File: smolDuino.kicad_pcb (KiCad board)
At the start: 2 copper layers, 68.6 x 53.3 mm, 63 parts, among them J1 Barrel_Jack_Switch, J2 USB_C_Receptacle_USB2.0, J3 2x3 SPI Header, J4 2x5 HV Outputs, J5 I^{2}C Connector, P1 CONN_01X01, P2 CONN_01X01, P3 CONN_01X01, P4 CONN_01X01, P5 Digital, P6 Power, P7 Digital, P8 Analog, Q1 AO3401A, SW1 Enable, SW2 Reset, U1 AP62250smol_A, U2 rp2040smol-c-unit, U3 74AHCT1G04, U4 Charj_smol, U5 AT24CS02-STUM, U6 SN74AHCT125N

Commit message: commit before I ruin too much
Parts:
- JP1: value 0 -> 0 DNP
- U6: footprint Package_DFN_QFN:Texas_S-PVQFN-N14 -> MikeFootprintLib:74x125_Texas_S-PVQFN-N14
- moved C4 0.29 mm to (141.9, 88.1)
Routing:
- net GND: track 89.1 -> 82.9 mm
- net /5V_IO15: track 6.67 -> 7.82 mm
- net /IO14: track 23.3 -> 24.3 mm
- net /EN: track 62.6 -> 62.1 mm
- net Net-(D3-Pad1): track 4.37 -> 4.90 mm

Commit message: Progress
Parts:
- removed the G*** at (174.0, 80.2)
- added C1: 47u, Capacitor_SMD:CP_Elec_6.3x5.4, F.Cu at (132.0, 121.9)
- added D4: Charge, LED_SMD:LED_0603_1608Metric, F.Cu at (127.9, 112.6)
- added R8: 2k, Resistor_SMD:R_0603_1608Metric, F.Cu at (142.7, 101.5)
- C2: renamed from C1; value 10uF -> 4u7
- C3: renamed from C2; value 100nF -> 100n
- C4, C5: value 100nF -> 100n
- D3: value Charge -> ChargeEn
- J1: value Barrel_Jack_Switch -> DC Barrel Jack
- U1: value AP62250smol_A -> AP62250smol; footprint MikePCBAs:AP62250smol_A -> MikePCBAs:AP62250smol_C
- moved SW1 46.5 mm to (176.5, 111.3), turned to 90 degrees
- moved MISC2 27.7 mm to (171.9, 111.2)
- moved ART1 23.6 mm to (174.0, 83.6)
- moved G*** 19.4 mm to (141.1, 118.9)
- moved D3 15.3 mm to (141.2, 101.5)
- moved G*** 8.49 mm to (125.0, 114.6)
- moved G*** 8.42 mm to (175.8, 103.9)
- moved R1 4.87 mm to (131.7, 108.3), turned to 180 degrees
- moved R3 4.38 mm to (128.7, 108.3), turned to 180 degrees
- moved F1 3.89 mm to (131.7, 113.6)
- moved R7 2.48 mm to (143.0, 107.3), turned to 90 degrees
- moved C6 2.30 mm to (140.4, 106.6), turned to 180 degrees
- moved U5 1.82 mm to (142.2, 104.4)
- moved JP1 1.18 mm to (129.4, 104.2)
- moved ART2 1.14 mm to (167.9, 106.2)
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- renumbered ART3 to ART2, ART4 to ART3, ART2 to ART4, C3 to C6, JP2 to JP1, JP3 to JP2, JP1 to JP3, R6 to R5, R7 to R6, R5 to R7, U6 to U3, U5 to U4, U3 to U5, U4 to U6
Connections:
- net Net-(C1-Pad2) renamed /V_{Bus}_{Fused}
- net Net-(F2-Pad1) renamed /V_{Bus}
- net Net-(J2-PadA5) renamed /CC1
- net Net-(J2-PadB5) renamed /CC2
- D3 pad 1: Net-(D3-Pad1) -> /~{ChargeEn}
- D3 pad 2: +5V -> Net-(D3-Pad2)
- U5 pad 4: Net-(U3-Pad4) -> /~{ChargeEn}
- U6 pad 5: Net-(U3-Pad4) -> /~{ChargeEn}
- U6 pad 6: Net-(D3-Pad1) -> /STAT
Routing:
- net /EN: track 62.1 -> 13.5 mm, vias 2 -> 0
- net /~{ChargeEn}: track 0.00 -> 28.9 mm, vias 0 -> 2
- net V_{High}: track 122.3 -> 145.2 mm
- net Net-(U3-Pad4): track 21.1 -> 0.00 mm
- net /VIN: track 35.0 -> 50.5 mm
- net /VIN_{Fused}: track 0.00 -> 12.9 mm
- net +5V: track 82.1 -> 91.8 mm
- net Net-(Q1-Pad1): track 51.7 -> 42.6 mm
- net /DC_{In}: track 12.3 -> 5.60 mm
- net V_{high_out}: track 18.2 -> 12.4 mm
- net Net-(D3-Pad1): track 4.90 -> 0.00 mm
- net /STAT: track 0.00 -> 3.80 mm
- net GND: track 82.9 -> 80.4 mm, vias 193 -> 201
- net /5V_MOSI1: track 23.4 -> 21.2 mm, vias 0 -> 1
- net /Reset: track 170.6 -> 172.6 mm
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- removed copper zone on F.Cu, net /VIN_{Fused}
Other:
- outline, holes or cut-outs redrawn

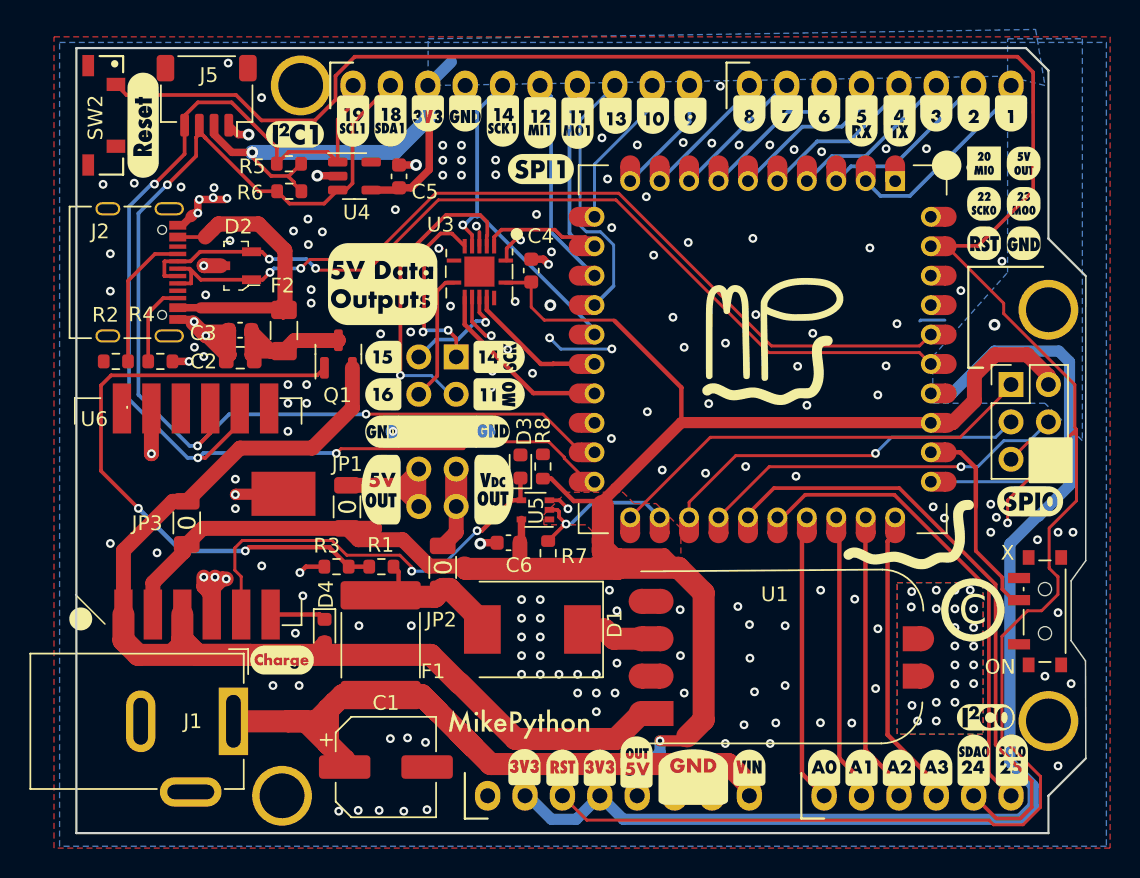
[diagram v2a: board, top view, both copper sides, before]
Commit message: More progress. Charjsmol is removed and integrated directly onto the board.
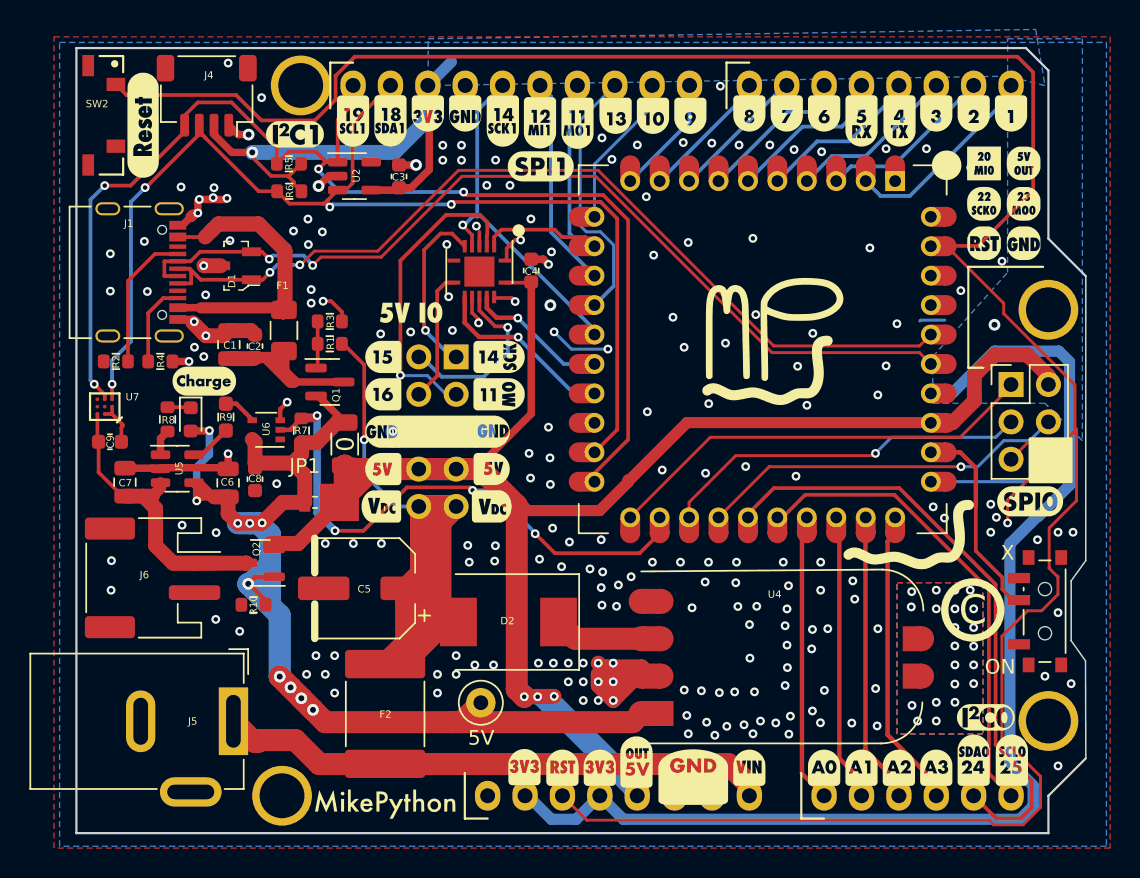
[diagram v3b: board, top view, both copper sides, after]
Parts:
- removed ART3, ART4: MPAnyArt, MikeArtworkLib:5vDataOutputsLabel
- removed the D3 at (141.2, 101.5)
- removed the JP1 at (129.4, 104.2)
- removed JP2: 0, MikeFootprintLib:R_0OHM_1206_3216Metric
- removed the U6 at (114.2, 111.5)
- added 5V: TestPoint, TestPoint:TestPoint_Loop_D2.50mm_Drill1.0mm_LowProfile, F.Cu at (138.5, 117.5)
- added C6: 10uF, Capacitor_SMD:C_0805_2012Metric, F.Cu at (121.3, 102.6)
- added C7: 10uF, Capacitor_SMD:C_0805_2012Metric, F.Cu at (114.3, 102.5)
- added C9: 1uF, Capacitor_SMD:C_0603_1608Metric, F.Cu at (113.3, 99.8)
- added D4: UPS120, MikeFootprintLib:UPS120_D_Powermite_AK, F.Cu at (128.2, 103.9)
- added G***: LOGO, LOGO, B.Cu at (135.5, 91.2)
- added G***: LOGO, LOGO, F.Cu at (134.0, 91.2)
- added J6: Battery Connector, Connector_JST:JST_PH_S2B-PH-SM4-TB_1x02-1MP_P2.00mm_Horizontal, F.Cu at (116.2, 109.0)
- added Q2: AO3401A, Package_TO_SOT_SMD:SOT-23, F.Cu at (123.5, 108.0)
- added R10: 100K, Resistor_SMD:R_0603_1608Metric, F.Cu at (123.0, 110.9)
- added R9: 4.7k, Resistor_SMD:R_0603_1608Metric_Pad0.98x0.95mm_HandSolder, F.Cu at (121.2, 98.1)
- added U5: MCP73831-2-OT, Package_TO_SOT_SMD:SOT-23-5, F.Cu at (117.8, 101.6)
- added U7: LC709203FXE-05MH, MikeFootprintLib:WLCSP9-1.60x1.76mm, F.Cu at (112.9, 97.4)
- R8: value 2k -> 1k
- U3: footprint MikeFootprintLib:74x125_Texas_S-PVQFN-N14 -> Package_DFN_QFN:Texas_S-PVQFN-N14
- moved R8 25.7 mm to (117.2, 98.3)
- moved G*** 19.7 mm to (119.7, 95.7)
- moved U6 19.1 mm to (123.9, 99.0)
- moved R7 18.7 mm to (126.3, 99.0)
- moved C8 17.8 mm to (123.1, 102.3), turned to -90 degrees
- moved D3 17.0 mm to (118.8, 98.3)
- moved R3 16.7 mm to (128.2, 91.6), turned to 0 degrees
- moved R1 15.5 mm to (128.2, 93.1)
- moved C5 12.2 mm to (130.6, 109.7), turned to 180 degrees
- moved JP1 12.0 mm to (129.2, 99.9), turned to 90 degrees
- moved G*** 10.6 mm to (132.0, 124.4)
- moved F2 4.68 mm to (132.0, 118.3)
- moved Q1 1.99 mm to (128.2, 95.7), turned to 0 degrees
- moved D2 1.70 mm to (140.4, 112.0)
- moved C2 1.48 mm to (123.1, 93.3), turned to 90 degrees
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- renumbered C2 to C1, C3 to C2, C5 to C3, C1 to C5, C6 to C8, D2 to D1, D1 to D2, D4 to D3, F2 to F1, F1 to F2, J2 to J1, J3 to J2, J4 to J3, J5 to J4, J1 to J5, JP3 to JP1, U2 to U1, U4 to U2, U1 to U4, U5 to U6
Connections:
- net /DC_{In} renamed /Power Supply/DC_{In}
- net /V_{Bus}_{Fused} renamed /V_{Bus}_{(Fused)}
- C5 pad 1: /VIN -> V_{DC}
- C8 pad 1: V_{High} -> +5V
- D2 pad 2: /VIN_{Fused} -> V_{DC}
- D3 pad 1: /STAT -> Net-(D3-Pad1)
- F2 pad 1: /VIN -> V_{IN}
- F2 pad 2: /VIN_{Fused} -> V_{DC}
- J3 pad 10: V_{high_out} -> V_{DC}
- J3 pad 7: V_{DC_out} -> V_{High}
- J3 pad 8: V_{high_out} -> V_{High}
- J3 pad 9: V_{DC_out} -> V_{DC}
- J5 pad 1: /VIN -> V_{IN}
- JP1 pad 1: +5V -> V_{High}
- JP1 pad 2: V_{High} -> +5V
- P6 pad 8: /VIN -> V_{IN}
- R1 pad 1: /VIN_{Fused} -> V_{DC}
- R7 pad 1: V_{High} -> +5V
- R8 pad 1: V_{High} -> /Battery Charging (Optional)/STAT
- R8 pad 2: Net-(D3-Pad2) -> Net-(D3-Pad1)
- U6 pad 4: /~{ChargeEn} -> /Battery Charging (Optional)/ProgSink
- U6 pad 5: V_{High} -> +5V
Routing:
- net V_{DC}: track 0.00 -> 58.3 mm, vias 0 -> 1
- net /VIN: track 50.5 -> 0.00 mm
- net Net-(Q1-Pad1): track 42.6 -> 3.05 mm, vias 2 -> 0
- net V_{IN}: track 0.00 -> 37.7 mm
- net /~{ChargeEn}: track 28.9 -> 0.00 mm, vias 2 -> 0
- net /ChargeEnable: track 10.5 -> 38.1 mm, vias 1 -> 4
- net +BATT: track 0.00 -> 19.6 mm
- net V_{High}: track 145.2 -> 131.7 mm, vias 1 -> 3
- net /VIN_{Fused}: track 12.9 -> 0.00 mm
- net V_{high_out}: track 12.4 -> 0.00 mm
- net V_{DC_out}: track 8.14 -> 0.00 mm
- net /IO19: track 79.0 -> 85.3 mm, vias 3 -> 4
- net /5V_IO15: track 7.49 -> 12.1 mm
- net /STAT: track 3.80 -> 0.00 mm
- net /Battery Charging (Optional)/PROG: track 0.00 -> 2.84 mm
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- removed copper zone on F.Cu, net V_{High}

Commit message: Rev C, I think
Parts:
- removed 5V: TestPoint, TestPoint:TestPoint_Loop_D2.50mm_Drill1.0mm_LowProfile
- removed the G*** at (116.6, 77.7)
- added JP1: Jumper_2_Bridged, Jumper:SolderJumper-2_P1.3mm_Bridged_Pad1.0x1.5mm, B.Cu at (170.8, 107.5)
- J3: footprint MikeConnectorFootprints:smolduino_2x05_header -> MikeConnectorFootprints:PinSocket_2x06_P2.54mm_Vertical
- JP2: renamed from JP1; footprint MikeFootprintLib:R_0OHM_1206_3216Metric -> Jumper:SolderJumper-2_P1.3mm_Open_TrianglePad1.0x1.5mm; moved to B.Cu
- R9: value 4.7k -> 2k; footprint Resistor_SMD:R_0603_1608Metric_Pad0.98x0.95mm_HandSolder -> Resistor_SMD:R_0603_1608Metric
- moved U2 10.3 mm to (119.6, 81.2)
- moved C3 9.69 mm to (123.2, 82.2), turned to 0 degrees
- moved R6 7.55 mm to (132.7, 80.6), turned to 180 degrees
- moved R5 4.26 mm to (129.7, 80.6)
- moved ART5 3.53 mm to (124.5, 110.4)
- moved R8 3.09 mm to (120.2, 97.4), turned to 0 degrees
- moved G*** 3.07 mm to (116.6, 96.0)
- moved C8 3.06 mm to (124.5, 99.6), turned to 180 degrees
- moved JP2 3.05 mm to (126.8, 101.7), turned to 180 degrees
- moved D4 2.90 mm to (128.7, 101.0), turned to 90 degrees
- moved D3 2.74 mm to (120.2, 95.9), turned to 180 degrees
- moved C5 2.29 mm to (130.6, 112.0)
- moved C7 2.10 mm to (116.4, 102.1)
- moved U6 1.85 mm to (123.5, 97.2), turned to -90 degrees
- moved R7 1.85 mm to (125.6, 97.3)
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- renumbered ART5 to ART3, ART6 to ART4, ART7 to ART5, ART8 to ART6
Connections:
- J3 pad 10: V_{DC} -> +5V
- J3 pad 9: V_{DC} -> +5V
- P6 pad 5: V_{High} -> +5V
- U1 pad 32: /EN -> /EN_Pin
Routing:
- net V_{High}: track 131.7 -> 83.1 mm, vias 3 -> 2
- net V_{DC}: track 58.3 -> 41.9 mm
- net +5V: track 89.4 -> 73.9 mm, vias 10 -> 11
- net /EN_Pin: track 0.00 -> 11.1 mm, vias 0 -> 1
- net /EN: track 13.5 -> 5.13 mm, vias 0 -> 1
- net /ChargeEnable: track 38.1 -> 31.9 mm, vias 4 -> 3
- net GND: track 82.3 -> 77.2 mm, vias 229 -> 286
- net /V_{Bus}_{(Fused)}: track 12.6 -> 7.89 mm
- net +3V3: track 117.4 -> 113.1 mm, vias 1 -> 2
- net +BATT: track 19.6 -> 15.4 mm
- net V_{IN}: track 37.7 -> 40.2 mm
- net /IO19: track 85.3 -> 83.3 mm
- net /Battery Charging (Optional)/STAT: track 1.78 -> 3.51 mm
- net /IO18: track 79.3 -> 78.2 mm
- net /Battery Charging (Optional)/PROG: track 2.84 -> 2.15 mm
- added copper zone on F.Cu, net +5V
- added copper zone on F.Cu, net +BATT
- added copper zone on F.Cu, net V_{DC}
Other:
- board text added: "By Mike in California December 2021"

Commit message: Adding gerbers
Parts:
- JP2: value 0 DNP -> Battery Protection Diode Bypass
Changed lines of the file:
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@@
     (pad "2" smd roundrect (at 1 -2.85 270) (size 1 3.5) (layers "F.Cu" "F.Paste" "F.Mask") (roundrect_rratio 0.25)
       (net 2 "GND") (pinfunction "Pin_2") (pintype "passive"))
-    (pad "MP" smd roundrect (at -3.35 2.9 270) (size 1.5 3.4) (layers "F.Cu" "F.Paste" "F.Mask") (roundrect_rratio 0.166667))
-    (pad "MP" smd roundrect (at 3.35 2.9 270) (size 1.5 3.4) (layers "F.Cu" "F.Paste" "F.Mask") (roundrect_rratio 0.166667))
+    (pad "MP" smd roundrect (at -3.35 2.9 270) (size 1.5 3.4) (layers "F.Cu" "F.Paste" "F.Mask") (roundrect_rratio 0.1666673333))
+    (pad "MP" smd roundrect (at 3.35 2.9 270) (size 1.5 3.4) (layers "F.Cu" "F.Paste" "F.Mask") (roundrect_rratio 0.1666673333))
     (model "${MODELSPATH}/JST/S2B-PH-SM4-TB.STEP"
       (offset (xyz -7.9 12.5 0))
@@
     (property "Sheetfile" "smolDuino.kicad_sch")
     (property "Sheetname" "")
-    (attr exclude_from_pos_files)
+    (property "exclude_from_bom" "")
+    (attr exclude_from_pos_files exclude_from_bom)
     (fp_text reference "JP2" (at 0 1.8) (layer "B.SilkS")
       (effects (font (size 1 1) (thickness 0.15)) (justify mirror))
     )
-    (fp_text value "0 DNP" (at 0 -1.9) (layer "B.Fab")
+    (fp_text value "Battery Protection Diode Bypass" (at 0 -1.9) (layer "B.Fab")
       (effects (font (size 1 1) (thickness 0.15)) (justify mirror))
     )
